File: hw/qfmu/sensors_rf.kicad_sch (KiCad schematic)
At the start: 32 parts, among them U11 MICRF219AAYQS-TR, U12 AS179-92LF, U13 MICRF113YM6-TR, U15 BMI088, Y3 13.52 MHz, Y4 13.52 MHz

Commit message: feat: finish motors, RF and power monitor
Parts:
- removed R2, R4: 0, Resistor_SMD:R_0805_2012Metric_Pad1.20x1.40mm_HandSolder, symbol Device:R
- added C54: 1.2p, Capacitor_SMD:C_0603_1608Metric_Pad1.08x0.95mm_HandSolder, symbol Device:C
- added C55: 1.5p, Capacitor_SMD:C_0603_1608Metric_Pad1.08x0.95mm_HandSolder, symbol Device:C
- added J2: Conn_Coaxial, Connector_Coaxial:SMA_Amphenol_901-144_Vertical, symbol Connector:Conn_Coaxial
- added L3: 39n, Inductor_SMD:L_0402_1005Metric_Pad0.77x0.64mm_HandSolder, symbol Device:L
- added L4: 33n, Inductor_SMD:L_0603_1608Metric_Pad1.05x0.95mm_HandSolder, symbol Device:L
- added Q25: AO3401A, Package_TO_SOT_SMD:SOT-23, symbol Transistor_FET:AO3401A
- added Q26: AO3400A, Package_TO_SOT_SMD:SOT-23, symbol Transistor_FET:AO3400A
- C52: footprint Capacitor_SMD:C_0805_2012Metric_Pad1.18x1.45mm_HandSolder -> Capacitor_SMD:C_0603_1608Metric_Pad1.08x0.95mm_HandSolder
- R1, R3: now fitted; now in the parts list
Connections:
- net +3.3V: now also Q25.3 (D); no longer U12.4 (V1), U12.6 (V2)
- net GND: now also J2.2 (Ext), L3.2, L4.2, Q26.2 (S)
- net at U11.3 (ANT): now also C54.2, L3.1
- net at U12.3 (J2): now also C55.1, L4.1
- net at U12.5 (J1): now also J2.1 (In)
- new net: Q25.2 (S), Q26.3 (D), U12.6 (V2)
- new net: C54.1, C55.2
- new net ANT_MODE: Q25.1 (G), Q26.1 (G), U12.4 (V1)
- no-connect marks 3 -> 5
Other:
- moved on the sheet: C41, C42, C43, C44, C45, C53, R15, R16, R18, R19, U11, Y3

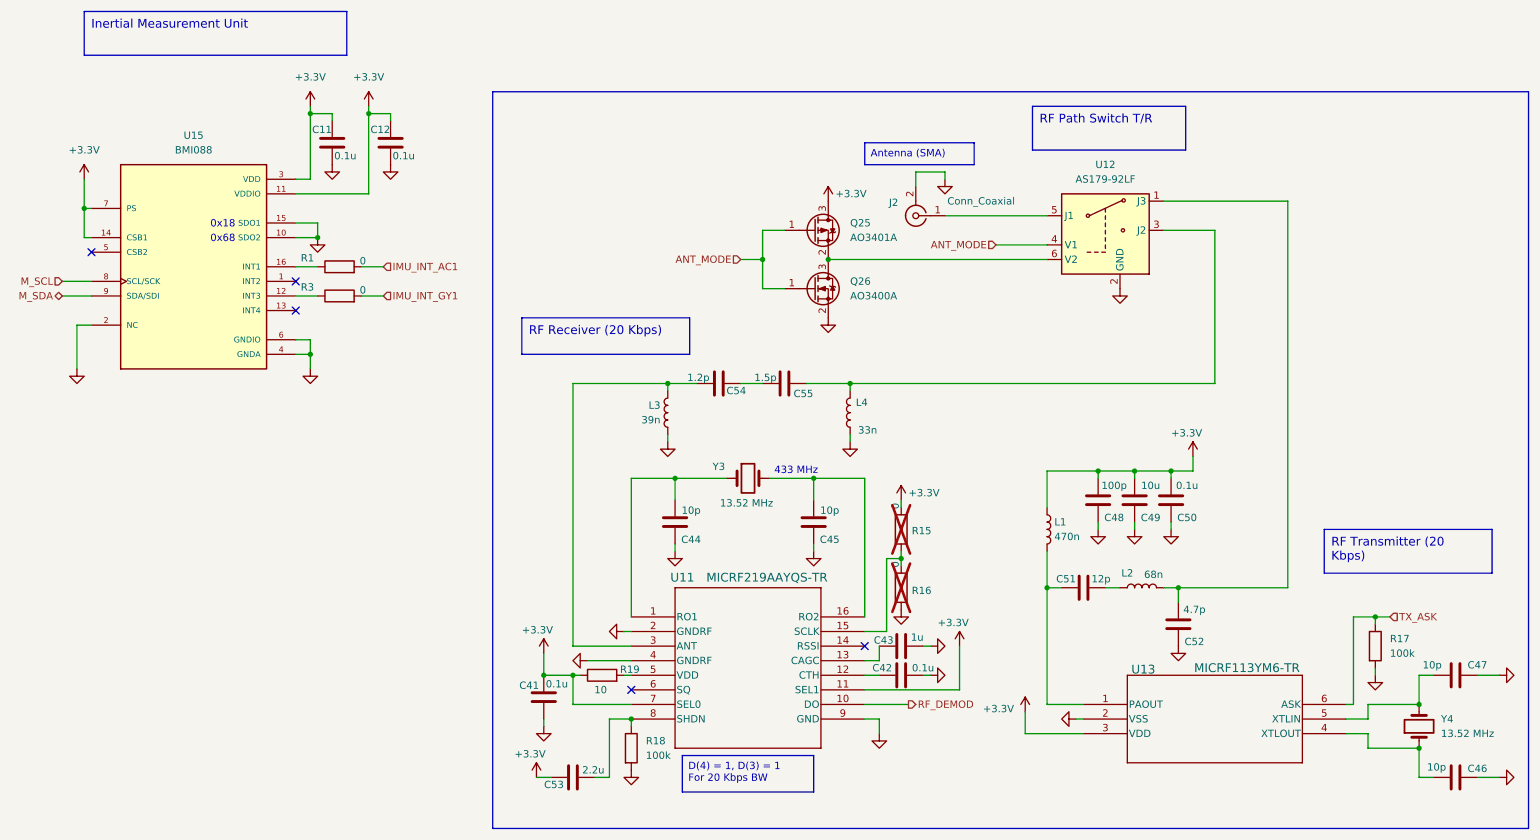
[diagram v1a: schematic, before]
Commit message: feat: start PCB design, define board outline and basic placement
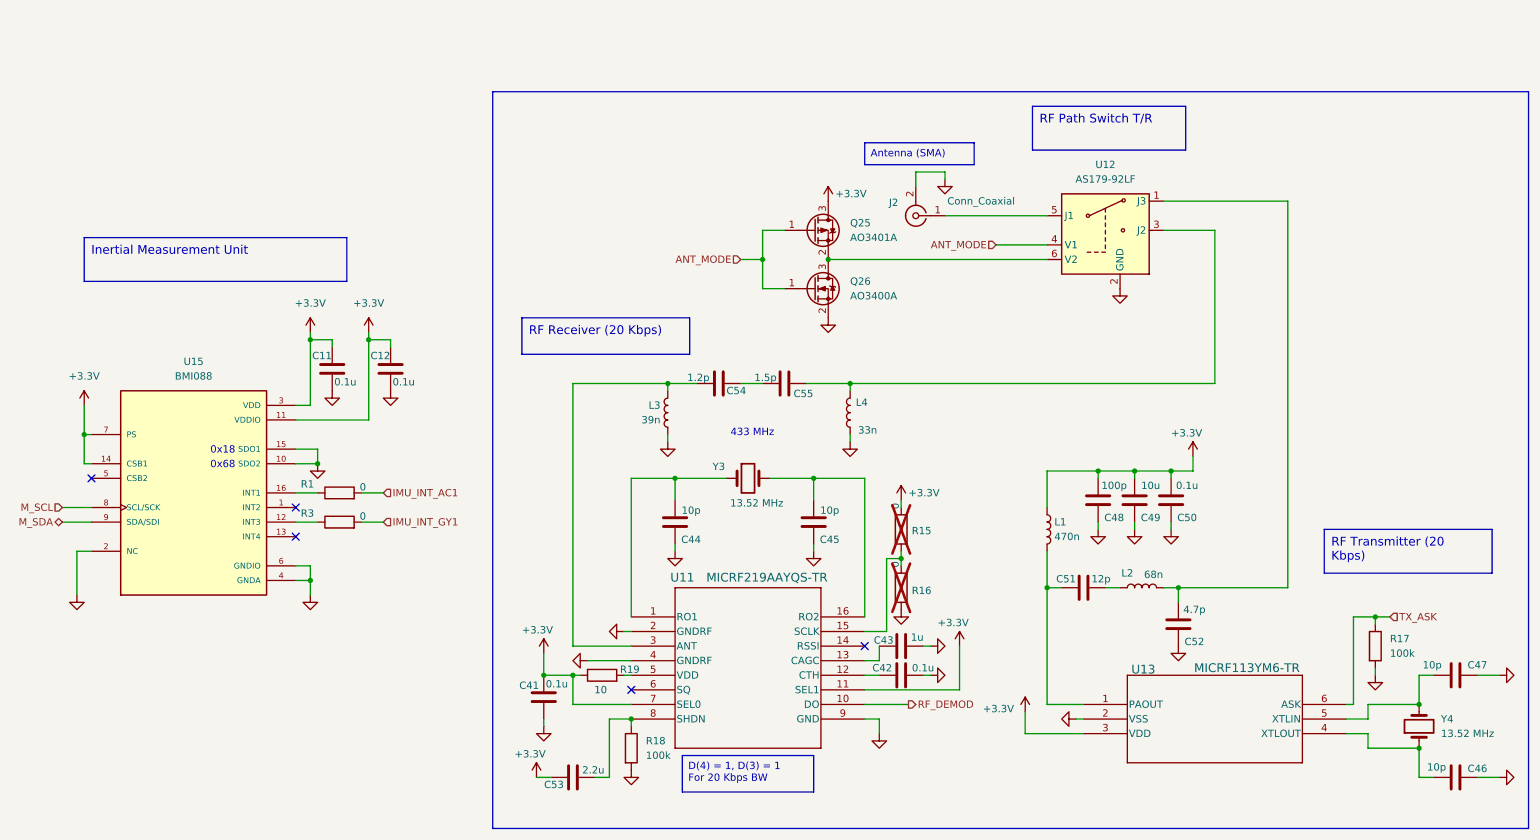
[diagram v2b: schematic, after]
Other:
- moved on the sheet: C11, C12, R1, R3
